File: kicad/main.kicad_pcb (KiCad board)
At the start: 2 copper layers, 11 parts, among them J1 Barrel_Jack, U1 74HC573, U2 27C512, U3 AS6C4008-55PCN, U4 8088_Min_Mode, U5 74HC573, U6 ATF16V8, U7 74LS73, U8 L7805, X1 15 MHz

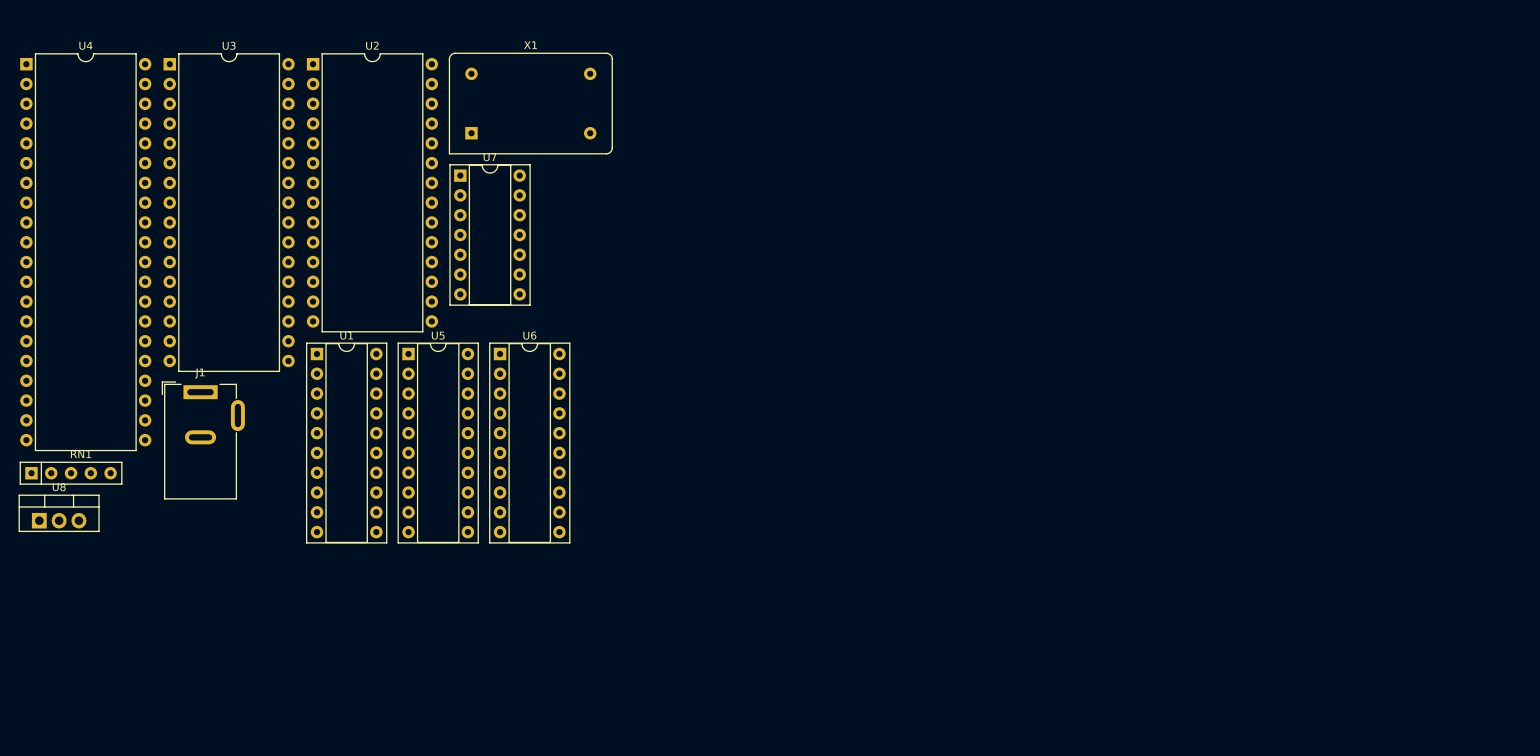
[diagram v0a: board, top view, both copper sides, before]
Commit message: Add interrupt controller & display
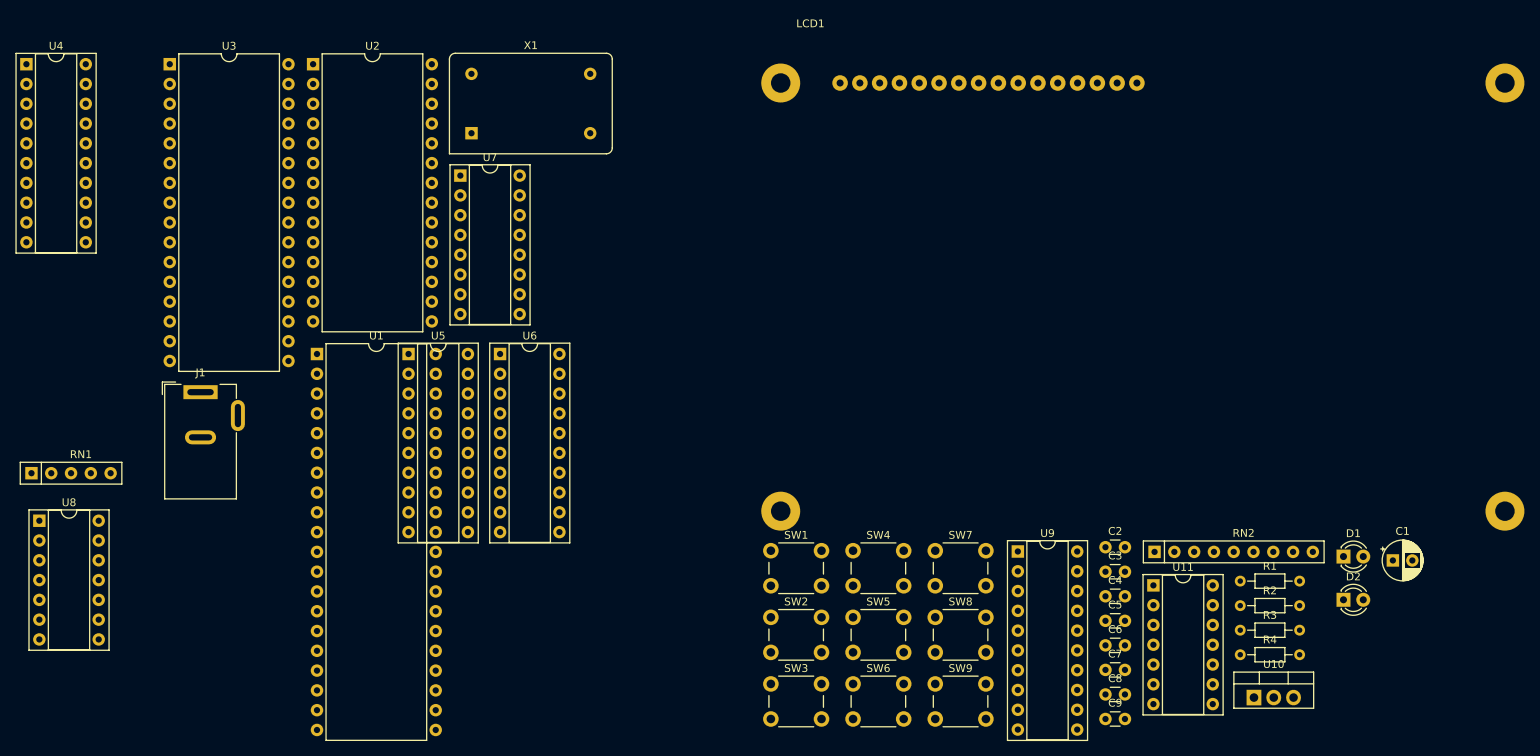
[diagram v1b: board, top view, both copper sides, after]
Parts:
- added C1: 10 uF, Capacitor_THT:CP_Radial_D5.0mm_P2.50mm, F.Cu at (203.5, 90.0)
- added C2: 0.1 uF, Capacitor_THT:C_Disc_D3.0mm_W1.6mm_P2.50mm, F.Cu at (166.6, 88.3)
- added C3: 0.1 uF, Capacitor_THT:C_Disc_D3.0mm_W1.6mm_P2.50mm, F.Cu at (166.6, 91.5)
- added C4: 0.1 uF, Capacitor_THT:C_Disc_D3.0mm_W1.6mm_P2.50mm, F.Cu at (166.6, 94.6)
- added C5: 0.1 uF, Capacitor_THT:C_Disc_D3.0mm_W1.6mm_P2.50mm, F.Cu at (166.6, 97.8)
- added C6: 0.1 uF, Capacitor_THT:C_Disc_D3.0mm_W1.6mm_P2.50mm, F.Cu at (166.6, 100.9)
- added C7: 0.1 uF, Capacitor_THT:C_Disc_D3.0mm_W1.6mm_P2.50mm, F.Cu at (166.6, 104.0)
- added C8: 0.1 uF, Capacitor_THT:C_Disc_D3.0mm_W1.6mm_P2.50mm, F.Cu at (166.6, 107.2)
- added C9: 0.1 uF, Capacitor_THT:C_Disc_D3.0mm_W1.6mm_P2.50mm, F.Cu at (166.6, 110.3)
- added D1: Power, LED_THT:LED_D3.0mm, F.Cu at (197.2, 89.5)
- added D2: Reset, LED_THT:LED_D3.0mm, F.Cu at (197.2, 95.0)
- added LCD1: ~, footprints:2004A-OLED, F.Cu at (122.4, 26.2)
- added R1: 100, Resistor_THT:R_Axial_DIN0204_L3.6mm_D1.6mm_P7.62mm_Horizontal, F.Cu at (183.9, 92.7)
- added R2: 10K, Resistor_THT:R_Axial_DIN0204_L3.6mm_D1.6mm_P7.62mm_Horizontal, F.Cu at (183.9, 95.8)
- added R3: 10K, Resistor_THT:R_Axial_DIN0204_L3.6mm_D1.6mm_P7.62mm_Horizontal, F.Cu at (183.9, 99.0)
- added R4: 10K, Resistor_THT:R_Axial_DIN0204_L3.6mm_D1.6mm_P7.62mm_Horizontal, F.Cu at (183.9, 102.1)
- added RN2: R_Network08, Resistor_THT:R_Array_SIP9, F.Cu at (172.9, 88.9)
- added SW1: Reset, Button_Switch_THT:SW_PUSH_6mm_H5mm, F.Cu at (123.7, 88.8)
- added SW2: A, Button_Switch_THT:SW_PUSH_6mm_H5mm, F.Cu at (123.7, 97.3)
- added SW3: B, Button_Switch_THT:SW_PUSH_6mm_H5mm, F.Cu at (123.7, 105.8)
- added SW4: C, Button_Switch_THT:SW_PUSH_6mm_H5mm, F.Cu at (134.2, 88.8)
- added SW5: D, Button_Switch_THT:SW_PUSH_6mm_H5mm, F.Cu at (134.2, 97.3)
- added SW6: E, Button_Switch_THT:SW_PUSH_6mm_H5mm, F.Cu at (134.2, 105.8)
- added SW7: F, Button_Switch_THT:SW_PUSH_6mm_H5mm, F.Cu at (144.8, 88.8)
- added SW8: G, Button_Switch_THT:SW_PUSH_6mm_H5mm, F.Cu at (144.8, 97.3)
- added SW9: H, Button_Switch_THT:SW_PUSH_6mm_H5mm, F.Cu at (144.8, 105.8)
- added U10: L7805, Package_TO_SOT_THT:TO-220-3_Vertical, F.Cu at (185.7, 107.6)
- added U11: 74LS73, Package_DIP:DIP-14_W7.62mm_Socket, F.Cu at (172.8, 93.2)
- added U9: 74HC244, Package_DIP:DIP-20_W7.62mm_Socket, F.Cu at (155.4, 88.8)
- U1: value 74HC573 -> KM1810VM88; footprint Package_DIP:DIP-20_W7.62mm_Socket -> Package_DIP:DIP-40_W15.24mm
- U2: value 27C512 -> W27C512
- U4: value 8088_Min_Mode -> 74HC573; footprint Package_DIP:DIP-40_W15.24mm -> Package_DIP:DIP-20_W7.62mm_Socket
- U7: value 74LS73 -> 74HC148; footprint Package_DIP:DIP-14_W7.62mm_Socket -> Package_DIP:DIP-16_W7.62mm_Socket
- U8: value L7805 -> 74HC00; footprint Package_TO_SOT_THT:TO-220-3_Vertical -> Package_DIP:DIP-14_W7.62mm_Socket
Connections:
- J1 pad 1: Net-(U8-IN) -> Net-(U10-IN)
- RN1 pad 5: Net-(RN1D-R4.2) -> unconnected-(RN1D-R4.2-Pad5)
- U1 pad 10: GND -> AD_{6}
- U1 pad 11: Net-(U1-Load) -> AD_{5}
- U1 pad 12: A_{7} -> AD_{4}
- U1 pad 13: A_{6} -> AD_{3}
- U1 pad 14: A_{5} -> AD_{2}
- U1 pad 15: A_{4} -> AD_{1}
- U1 pad 16: A_{3} -> AD_{0}
- U1 pad 17: A_{2} -> Net-(RN1B-R2.2)
- U1 pad 18: A_{1} -> INTR
- U1 pad 19: A_{0} -> CLK
- U1 pad 2: AD_{0} -> A_{14}
- U1 pad 20: +5V -> GND
- U1 pad 3: AD_{1} -> A_{13}
- U1 pad 4: AD_{2} -> A_{12}
- U1 pad 5: AD_{3} -> A_{11}
- U1 pad 6: AD_{0} -> A_{10}
- U1 pad 7: AD_{5} -> A_{9}
- U1 pad 8: AD_{6} -> A_{8}
- U3 pad 29: ~{RD} -> ~{WR}
- U4 pad 10: AD_{6} -> GND
- U4 pad 11: AD_{5} -> ALE
- U4 pad 12: AD_{0} -> A_{7}
- U4 pad 13: AD_{3} -> A_{6}
- U4 pad 14: AD_{2} -> A_{5}
- U4 pad 15: AD_{1} -> A_{4}
- U4 pad 16: AD_{0} -> A_{3}
- U4 pad 17: Net-(RN1B-R2.2) -> A_{2}
- U4 pad 18: Net-(RN1C-R3.2) -> A_{1}
- U4 pad 19: CLK -> A_{0}
- U4 pad 2: A_{14} -> AD_{0}
- U4 pad 20: GND -> +5V
- U4 pad 3: A_{13} -> AD_{1}
- U4 pad 4: A_{12} -> AD_{2}
- U4 pad 5: A_{11} -> AD_{3}
- U4 pad 6: A_{10} -> AD_{4}
- U4 pad 7: A_{9} -> AD_{5}
- U4 pad 8: A_{8} -> AD_{6}
- U5 pad 11: Net-(U1-Load) -> ALE
- U5 pad 2: Net-(U4-A16/S3) -> AS_{16}
- U5 pad 3: Net-(U4-A17/S4) -> AS_{17}
- U5 pad 4: Net-(U4-A18/S5) -> AS_{18}
- U5 pad 5: Net-(U4-A19/S6) -> AS_{19}
- U6 pad 1: A_{16} -> A_{8}
- U6 pad 17: IO~{EN} -> LCDEN
- U6 pad 2: A_{17} -> A_{9}
- U6 pad 3: A_{18} -> A_{10}
- U6 pad 4: A_{19} -> A_{16}
- U6 pad 5: IO/~{M} -> A_{17}
- U6 pad 6: unconnected-(U6-I6-Pad6) -> A_{18}
- U6 pad 7: unconnected-(U6-I7-Pad7) -> A_{19}
- U6 pad 8: unconnected-(U6-I8-Pad8) -> IO/~{M}
- U6 pad 9: unconnected-(U6-I9-Pad9) -> ALE
- U7 pad 1: Net-(U7A-C) -> ~{INT3}
- U7 pad 10: Net-(U7A-C) -> ~{INT7}
- U7 pad 11: GND -> ~{INT6}
- U7 pad 12: CLK -> ~{INT5}
- U7 pad 13: Net-(U7A-J) -> ~{INT4}
- U7 pad 14: Net-(U7A-Q) -> Net-(U7-GS)
- U7 pad 2: +5V -> ~{INT2}
- U7 pad 3: +5V -> ~{INT1}
- U7 pad 4: +5V -> ~{INT0}
- U7 pad 5: Net-(U7A-C) -> GND
- U7 pad 6: +5V -> Net-(U7-S2)
- U7 pad 7: Net-(U7A-J) -> Net-(U7-S1)
- U7 pad 8: unconnected-(U7A-~{Q}-Pad8) -> GND
- U7 pad 9: Net-(U7A-Q) -> Net-(U7-S0)
- U8 pad 1: Net-(U8-IN) -> Net-(U7-GS)
- U8 pad 2: GND -> Net-(U7-GS)
- U8 pad 3: +5V -> INTR
- X1 pad 8: Net-(U7A-C) -> Net-(U11A-C)

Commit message: Add parallel port
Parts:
- removed SW6: E, Button_Switch_THT:SW_PUSH_6mm_H5mm
- removed SW7: F, Button_Switch_THT:SW_PUSH_6mm_H5mm
- removed SW8: G, Button_Switch_THT:SW_PUSH_6mm_H5mm
- removed SW9: H, Button_Switch_THT:SW_PUSH_6mm_H5mm
- removed X1: 15 MHz, Oscillator:Oscillator_DIP-14
- added C10: 0.1 uF, Capacitor_THT:C_Disc_D3.0mm_W1.6mm_P2.50mm, F.Cu at (167.7, 116.8)
- added U12: 8255, Package_DIP:DIP-40_W15.24mm_Socket, F.Cu at (101.6, 63.5)
- RN2: value R_Network08 -> R_Network04; footprint Resistor_THT:R_Array_SIP9 -> Resistor_THT:R_Array_SIP5
- U11: value 74LS73 -> 15 MHz; footprint Package_DIP:DIP-14_W7.62mm_Socket -> footprints:Oscillator_DIP-8-14
- moved U11 101.4 mm to (94.0, 29.4)
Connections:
- LCD1 pad 10: AD_{3} -> Net-(LCD1-D_{3})
- LCD1 pad 11: AD_{4} -> Net-(LCD1-D_{4})
- LCD1 pad 12: AD_{5} -> Net-(LCD1-D_{5})
- LCD1 pad 13: AD_{6} -> Net-(LCD1-D_{6})
- LCD1 pad 14: AD_{7} -> Net-(LCD1-D_{7})
- LCD1 pad 4: AD_{0} -> Net-(LCD1-RS)
- LCD1 pad 5: ~{WR} -> Net-(LCD1-R~{W})
- LCD1 pad 6: LCDEN -> Net-(LCD1-E)
- LCD1 pad 7: AD_{0} -> Net-(LCD1-D_{0})
- LCD1 pad 8: AD_{1} -> Net-(LCD1-D_{1})
- LCD1 pad 9: AD_{2} -> Net-(LCD1-D_{2})
- U11 pad 1: Net-(U11A-C) -> unconnected-(U11-EN-Pad1)
- U11 pad 10: Net-(U11A-C) -> Net-(U11-OUT)
- U11 pad 12: CLK -> +5V
- U11 pad 13: Net-(U11A-J) -> +5V
- U11 pad 14: Net-(U11A-Q) -> +5V
- U11 pad 2: +5V -> unconnected-(U11-Pad2)
- U11 pad 3: +5V -> unconnected-(U11-Pad3)
- U11 pad 5: Net-(U11A-C) -> GND
- U11 pad 6: +5V -> GND
- U11 pad 7: Net-(U11A-J) -> GND
- U11 pad 8: unconnected-(U11A-~{Q}-Pad8) -> Net-(U11-OUT)
- U11 pad 9: Net-(U11A-Q) -> Net-(U11-OUT)
- U6 pad 1: A_{8} -> Net-(U11-OUT)
- U6 pad 13: unconnected-(U6-IO7-Pad13) -> Net-(U6-IO7)
- U6 pad 17: LCDEN -> IO~{EN}
- U6 pad 2: A_{9} -> A_{8}
- U6 pad 3: A_{10} -> A_{9}
- U6 pad 4: A_{16} -> A_{10}
- U6 pad 5: A_{17} -> A_{16}
- U6 pad 6: A_{18} -> A_{17}
- U6 pad 7: A_{19} -> A_{18}
- U6 pad 8: IO/~{M} -> A_{19}
- U6 pad 9: ALE -> IO/~{M}
- U7 pad 10: ~{INT7} -> +5V
- U7 pad 11: ~{INT6} -> +5V
- U7 pad 12: ~{INT5} -> +5V
- U7 pad 13: ~{INT4} -> +5V
- U8 pad 4: unconnected-(U8-Pad4) -> Net-(U6-IO7)
- U8 pad 5: unconnected-(U8-Pad5) -> Net-(U6-IO7)
- U8 pad 6: unconnected-(U8-Pad6) -> CLK

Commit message: Add Freerouting PCB
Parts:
- removed C1: 10 uF, Capacitor_THT:CP_Radial_D5.0mm_P2.50mm
- removed R1: 100, Resistor_THT:R_Axial_DIN0204_L3.6mm_D1.6mm_P7.62mm_Horizontal
- removed R4: 10K, Resistor_THT:R_Axial_DIN0204_L3.6mm_D1.6mm_P7.62mm_Horizontal
- removed RN2: R_Network04, Resistor_THT:R_Array_SIP5
- removed SW2: A, Button_Switch_THT:SW_PUSH_6mm_H5mm
- removed SW3: B, Button_Switch_THT:SW_PUSH_6mm_H5mm
- removed SW4: C, Button_Switch_THT:SW_PUSH_6mm_H5mm
- removed SW5: D, Button_Switch_THT:SW_PUSH_6mm_H5mm
- removed U9: 74HC244, Package_DIP:DIP-20_W7.62mm_Socket
- added BAR1: HDSP-4830_2, Display:HDSP-4830, F.Cu at (77.5, -12.7)
- added C11: 0.1 uF, Capacitor_THT:C_Disc_D3.0mm_W1.6mm_P2.50mm, F.Cu at (20.7, -26.7)
- added H1: MountingHole, footprints:Hole_2.5x4, F.Cu at (19.1, -14.0)
- added H2: MountingHole, footprints:Hole_2.5x4, F.Cu at (130.8, -14.0)
- added RN3: 330R, Resistor_THT:R_Array_SIP9, F.Cu at (77.5, -25.4)
- added RN4: 5K, Resistor_THT:R_Array_SIP9, F.Cu at (106.7, -25.4)
- added SW6: SW_DIP_x08, Button_Switch_THT:SW_DIP_SPSTx08_Slide_9.78x22.5mm_W7.62mm_P2.54mm, F.Cu at (106.7, -12.7)
- added U13: 74HC273, Package_DIP:DIP-20_W7.62mm_Socket, F.Cu at (77.5, -30.5)
- added U14: 74HC244, Package_DIP:DIP-20_W7.62mm_Socket, F.Cu at (106.7, -30.5)
- C10, C2, C4, C5, C7, C8, C9: footprint Capacitor_THT:C_Disc_D3.0mm_W1.6mm_P2.50mm -> footprints:C_Disc_Long
- C6: footprint Capacitor_THT:C_Disc_D3.0mm_W1.6mm_P2.50mm -> footprints:C_Disc_VeryLong
- U2: footprint Package_DIP:DIP-28_W15.24mm -> footprints:ZIF28
- U7: value 74HC148 -> DS1813-5+; footprint Package_DIP:DIP-16_W7.62mm_Socket -> Package_TO_SOT_THT:TO-92L_Inline_Wide
- moved C2 217.4 mm to (40.6, -88.9)
- moved C3 211.5 mm to (25.4, -66.0), turned to -90 degrees
- moved C4 209.1 mm to (87.6, -99.1), turned to -90 degrees
- moved U10 203.8 mm to (123.2, -86.4)
- moved C6 199.9 mm to (108.0, -90.2), turned to -90 degrees
- moved C7 187.8 mm to (53.3, -45.7)
- moved C5 183.0 mm to (87.6, -67.3), turned to -90 degrees
- moved D2 181.8 mm to (129.5, -73.7)
- moved J1 180.4 mm to (126.3, -95.2), turned to 180 degrees
- moved D1 179.7 mm to (121.9, -73.7), turned to 180 degrees
- moved R3 178.1 mm to (127.0, -69.8), turned to 90 degrees
- moved R2 176.0 mm to (124.5, -69.8), turned to 90 degrees
- moved LCD1 170.1 mm to (17.8, -108.0)
- moved U5 167.8 mm to (83.8, -104.1)
- moved C8 167.7 mm to (114.3, -52.1), turned to 180 degrees
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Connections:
- RN1 pad 5: unconnected-(RN1D-R4.2-Pad5) -> Net-(RN1D-R4.2)
- SW1 pad 1: Net-(R1-Pad2) -> Net-(U7-~{RST})
- SW1 pad 2: RES -> GND
- U1 pad 18: INTR -> Net-(RN1C-R3.2)
- U1 pad 24: ~{INTA} -> unconnected-(U1-~{INTA}-Pad24)
- U1 pad 33: Net-(RN1C-R3.2) -> Net-(RN1D-R4.2)
- U12 pad 35: IO~{EN} -> RES
- U4 pad 12: A_{7} -> A_{0}
- U4 pad 13: A_{6} -> A_{1}
- U4 pad 14: A_{5} -> A_{2}
- U4 pad 15: A_{4} -> A_{3}
- U4 pad 16: A_{3} -> A_{4}
- U4 pad 17: A_{2} -> A_{5}
- U4 pad 18: A_{1} -> A_{6}
- U4 pad 19: A_{0} -> A_{7}
- U4 pad 2: AD_{0} -> AD_{7}
- U4 pad 3: AD_{1} -> AD_{6}
- U4 pad 4: AD_{2} -> AD_{5}
- U4 pad 5: AD_{3} -> AD_{4}
- U4 pad 6: AD_{4} -> AD_{3}
- U4 pad 7: AD_{5} -> AD_{2}
- U4 pad 8: AD_{6} -> AD_{1}
- U4 pad 9: AD_{7} -> AD_{0}
- U6 pad 15: unconnected-(U6-IO5-Pad15) -> IO~{EN}
- U6 pad 16: unconnected-(U6-IO4-Pad16) -> IN~{EN}
- U6 pad 17: IO~{EN} -> OUT~{EN}
- U6 pad 3: A_{9} -> A_{16}
- U6 pad 4: A_{10} -> A_{17}
- U6 pad 5: A_{16} -> A_{18}
- U6 pad 6: A_{17} -> A_{19}
- U6 pad 7: A_{18} -> ~{RD}
- U6 pad 8: A_{19} -> ~{WR}
- U7 pad 1: ~{INT3} -> Net-(U7-~{RST})
- U7 pad 2: ~{INT2} -> +5V
- U7 pad 3: ~{INT1} -> GND
- U8 pad 1: Net-(U7-GS) -> Net-(U6-IO7)
- U8 pad 10: unconnected-(U8-Pad10) -> Net-(U7-~{RST})
- U8 pad 2: Net-(U7-GS) -> Net-(U6-IO7)
- U8 pad 3: INTR -> CLK
- U8 pad 4: Net-(U6-IO7) -> RES
- U8 pad 5: Net-(U6-IO7) -> RES
- U8 pad 6: CLK -> Net-(U13-~{Mr})
- U8 pad 8: unconnected-(U8-Pad8) -> RES
- U8 pad 9: unconnected-(U8-Pad9) -> Net-(U7-~{RST})
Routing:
- net GND: track 0.00 -> 553.8 mm
- net +5V: track 0.00 -> 445.0 mm
- net AD_{6}: track 0.00 -> 217.2 mm, vias 0 -> 1
- net AD_{7}: track 0.00 -> 216.3 mm, vias 0 -> 2
- net ~{RD}: track 0.00 -> 200.4 mm, vias 0 -> 3
- net AD_{4}: track 0.00 -> 197.5 mm
- net AD_{5}: track 0.00 -> 191.4 mm
- net AD_{3}: track 0.00 -> 188.2 mm
- net A_{0}: track 0.00 -> 187.3 mm, vias 0 -> 2
- net A_{1}: track 0.00 -> 182.9 mm, vias 0 -> 4
- net AD_{2}: track 0.00 -> 181.4 mm, vias 0 -> 3
- net A_{5}: track 0.00 -> 179.4 mm, vias 0 -> 2
- net AD_{0}: track 0.00 -> 175.4 mm, vias 0 -> 2
- net A_{15}: track 0.00 -> 165.9 mm, vias 0 -> 1
- net AD_{1}: track 0.00 -> 164.8 mm, vias 0 -> 1
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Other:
- board outline added: 119.4 x 99.1 mm
- board text added: "88"
- board text added: "Андрій Дунай v0.1, Вересень 2023 <a@dun.ai>"

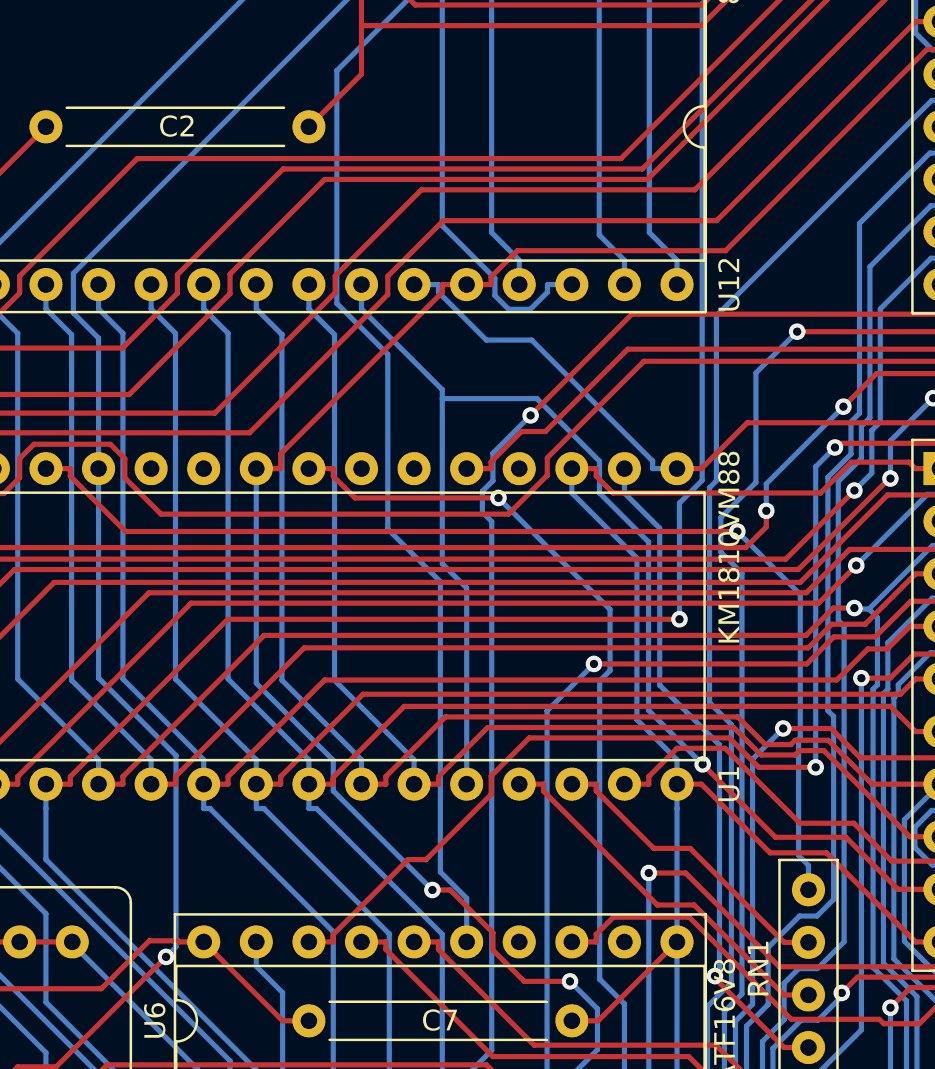
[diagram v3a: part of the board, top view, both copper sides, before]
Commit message: Fix HOLD, INT & address decoder equations
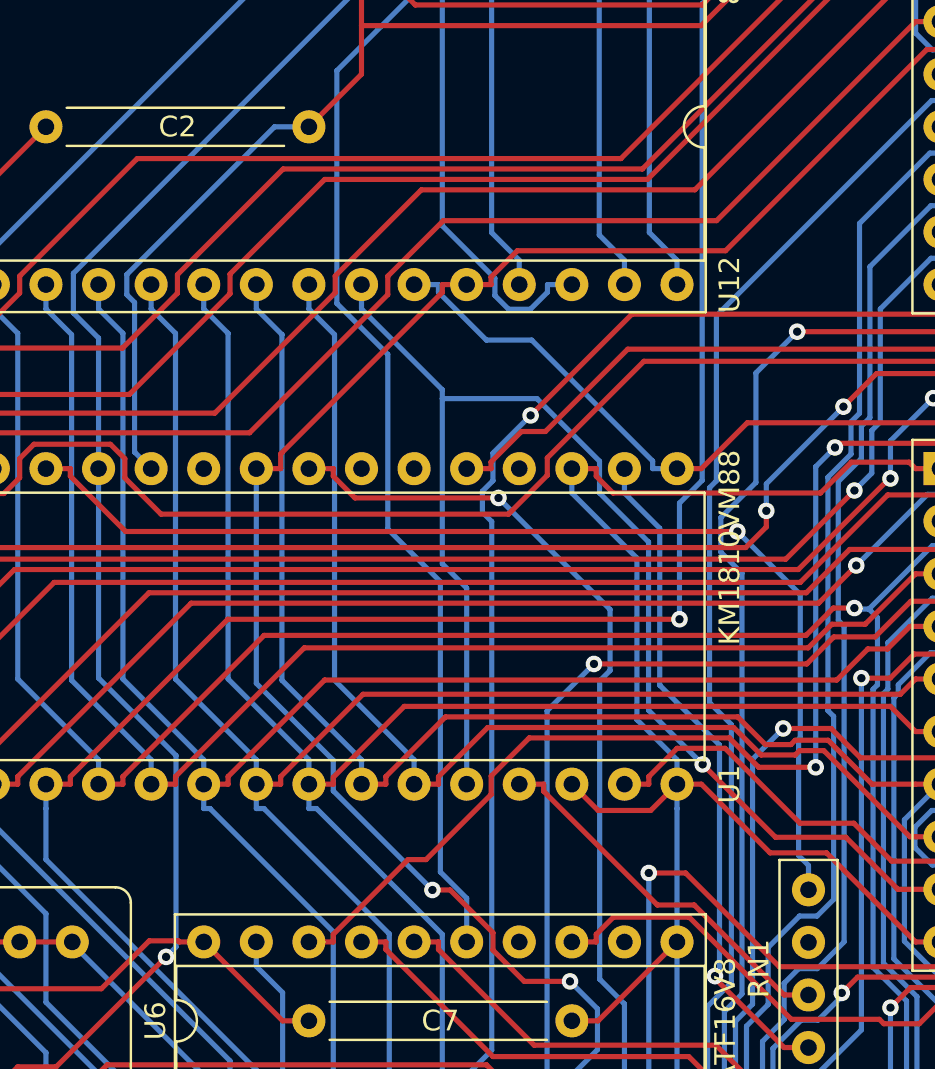
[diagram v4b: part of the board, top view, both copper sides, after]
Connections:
- RN1 pad 4: Net-(RN1C-R3.2) -> unconnected-(RN1C-R3.2-Pad4)
- U1 pad 18: Net-(RN1C-R3.2) -> GND
- U1 pad 31: unconnected-(U1-HOLD-Pad31) -> GND
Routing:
- net GND: track 553.8 -> 581.5 mm
- net Net-(RN1C-R3.2): track 14.8 -> 0.00 mm
